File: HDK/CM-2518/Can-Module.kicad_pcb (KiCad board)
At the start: 2 copper layers, 34.5 x 14.2 mm, 12 parts, among them J101 Can Connect, J102 Can Connect, SW101 SW_DIP_x01, U101 SN65HVD230, U102 MCP2518FD, Y101 20MHz

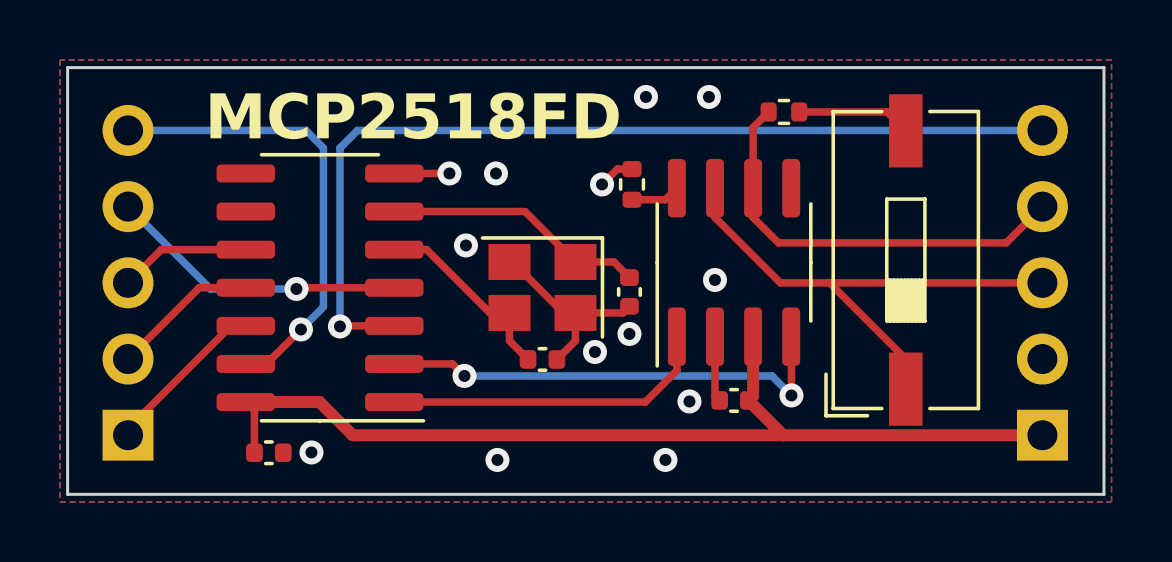
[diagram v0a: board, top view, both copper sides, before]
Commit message: updated CM-2518FD Module
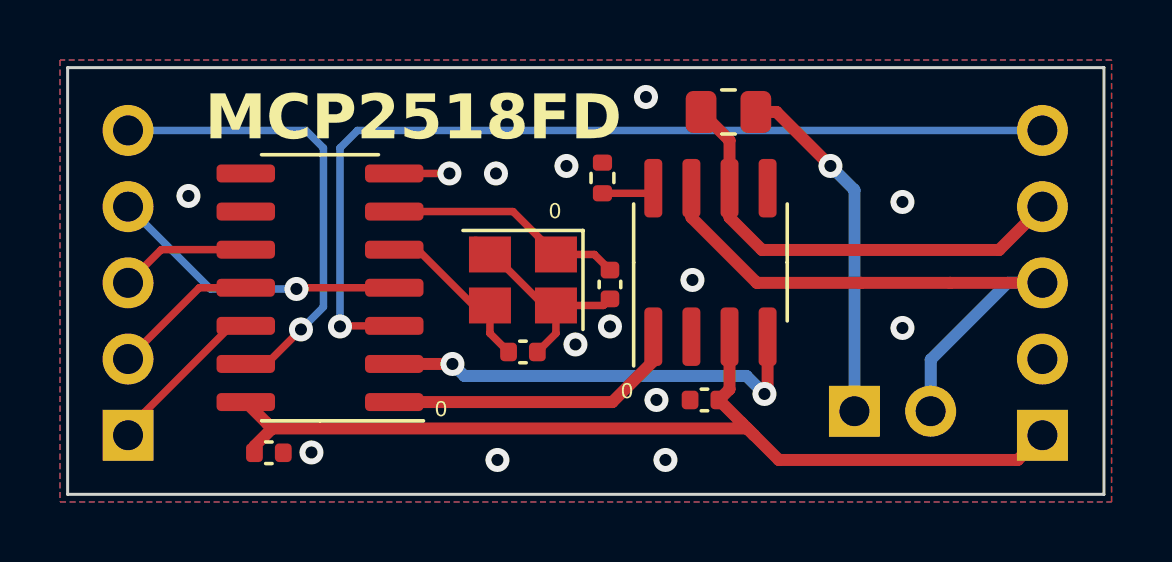
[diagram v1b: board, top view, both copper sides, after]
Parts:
- removed SW101: SW_DIP_x01, Button_Switch_SMD:SW_DIP_SPSTx01_Slide_9.78x4.72mm_W8.61mm_P2.54mm
- added J103: Can Termination, NVF-Kicad:PinHeader_1x02_P2.54mm_Horizontal, F.Cu at (172.0, 96.8)
- C103, C104: value 10p -> 20p
- R102: footprint Resistor_SMD:R_0402_1005Metric -> Resistor_SMD:R_0805_2012Metric
- Y101: value 20MHz -> 40MHz
- moved R102 1.85 mm to (167.8, 86.8)
- moved R101 1.01 mm to (163.6, 89.0)
- moved C102 0.99 mm to (167.0, 96.4)
- moved U101 0.79 mm to (167.2, 91.8)
- moved C103 0.70 mm to (163.8, 92.5)
- moved C104 0.70 mm to (160.9, 94.8)
- moved Y101 0.70 mm to (160.9, 92.4)
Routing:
- net Net-(J103-Pin_1): track 3.81 -> 11.7 mm, vias 0 -> 1
- net /CAN_H: track 16.4 -> 20.1 mm
- net GND: track 13.3 -> 9.90 mm, vias 13 -> 14
- net /CAN_L: track 14.2 -> 15.4 mm
- net /CAN_TX: track 11.0 -> 10.0 mm
- net /CAN_RX: track 15.6 -> 14.7 mm
- net /OSC_OUT: track 6.52 -> 5.77 mm
- net /OSC_IN: track 8.75 -> 8.00 mm
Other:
- board text added: "0"

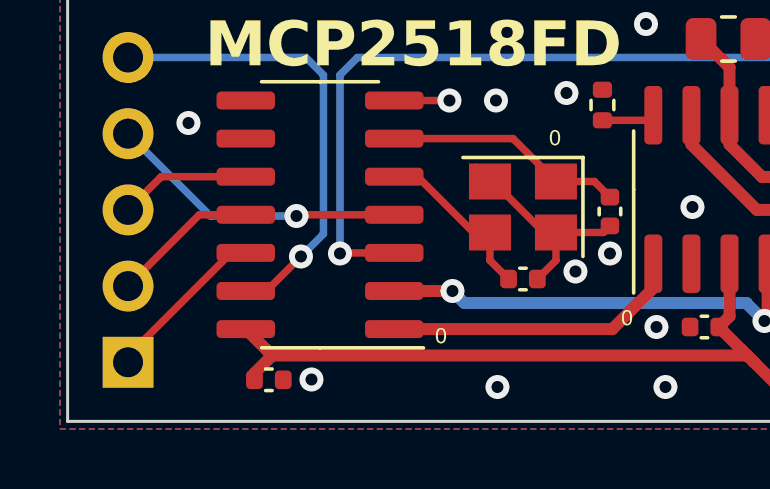
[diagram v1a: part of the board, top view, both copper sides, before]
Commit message: updated CM2515
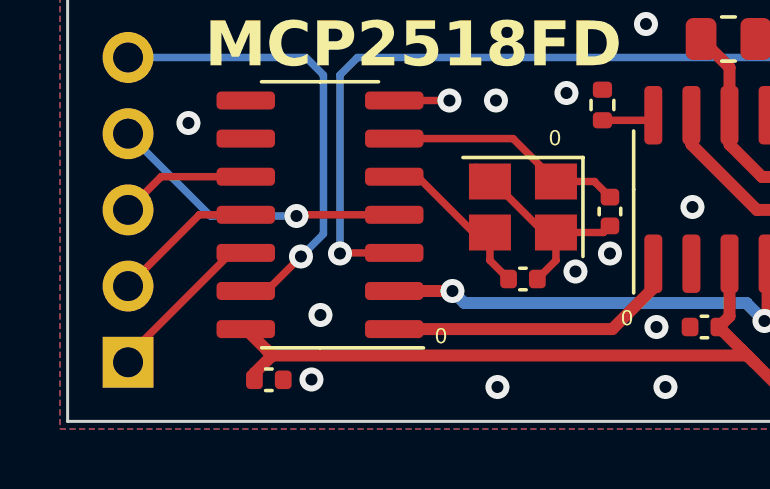
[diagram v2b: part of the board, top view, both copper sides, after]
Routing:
- net GND: vias 14 -> 15
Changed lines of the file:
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@@
         (effects (font (size 1 1) (thickness 0.15)))
     )
-    (fp_text value "20p" (at 0 1.16 90) (layer "F.Fab")
+    (fp_text value "20p" (at 1.25 0.05 -180) (layer "F.Fab")
         (effects (font (size 1 1) (thickness 0.15)))
     )
@@
         (effects (font (size 1 1) (thickness 0.15)))
     )
-    (fp_text value "SN65HVD230" (at 0 3.4 90) (layer "F.Fab")
-        (effects (font (size 1 1) (thickness 0.15)))
-    )
-    (fp_text user "${REFERENCE}" (at 0 0 90) (layer "F.Fab")
+    (fp_text value "SN65HVD230" (at 2.616 2.4 180) (layer "F.Fab")
+        (effects (font (size 1 1) (thickness 0.15)))
+    )
+    (fp_text user "${REFERENCE}" (at 0 0 180) (layer "F.Fab")
         (effects (font (size 0.98 0.98) (thickness 0.15)))
     )
@@
         (effects (font (size 1 1) (thickness 0.15)))
     )
-    (fp_text value "10K" (at 0 1.17 90) (layer "F.Fab")
+    (fp_text value "10K" (at -1.4 0 -180) (layer "F.Fab")
         (effects (font (size 1 1) (thickness 0.15)))
     )
@@
   (via (at 165.7 98.4) (size 0.8) (drill 0.4) (layers "F.Cu" "B.Cu") (free) (net 2))
   (via (at 162.4 88.6) (size 0.8) (drill 0.4) (layers "F.Cu" "B.Cu") (free) (net 2))
+  (via (at 154.2 96) (size 0.8) (drill 0.4) (layers "F.Cu" "B.Cu") (free) (net 2))
   (via (at 163.85 93.95) (size 0.8) (drill 0.4) (layers "F.Cu" "B.Cu") (free) (net 2))
   (via (at 166.6 92.4) (size 0.8) (drill 0.4) (layers "F.Cu" "B.Cu") (free) (net 2))

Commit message: updated can-module
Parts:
- removed J102: Can Connect, Connector_PinHeader_2.54mm:PinHeader_1x05_P2.54mm_Vertical
- J101: value Can Connect -> MCP251X; footprint Connector_PinHeader_2.54mm:PinHeader_1x05_P2.54mm_Vertical -> NVF-Kicad:Can-Module-CM251X; moved to F.Cu
- moved C102 63.5 mm to (104.0, 103.9)
- moved C103 63.5 mm to (100.8, 100.1)
- moved J103 63.5 mm to (109.0, 104.3)
- moved R101 63.5 mm to (100.6, 96.5)
- moved R102 63.5 mm to (104.8, 94.3)
- moved U101 63.5 mm to (91.2, 100.2)
- moved C101 63.5 mm to (89.5, 105.7)
- moved C104 63.5 mm to (97.9, 102.3)
- moved U102 63.5 mm to (104.2, 99.3)
- moved Y101 63.5 mm to (97.9, 99.9)
- moved J101 47.8 mm to (100.0, 100.0)
- renumbered U102 to U101, U101 to U102
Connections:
- J101 pad 1: /SPI_MISO -> /~{CS}
- J101 pad 2: /SPI_MOSI -> /CAN_IRQ
- J101 pad 4: /CAN_IRQ -> /SPI_MOSI
- J101 pad 5: /~{CS} -> /SPI_MISO
- R102 pad 1: Net-(J103-Pin_1) -> Net-(J102-Pin_1)
